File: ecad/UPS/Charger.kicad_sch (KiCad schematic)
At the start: 65 parts, among them J1 Barrel_Jack, J2 Conn_01x02_Socket, Q1 Q_PMOS, Q2 Q_PMOS_DGS, Q6 Q_NMOS_GDS, Q7 Q_NMOS_GDS, Q8 Q_NMOS_GDS, Q9 Q_NMOS_GDS, U1 BQ25730RSNR

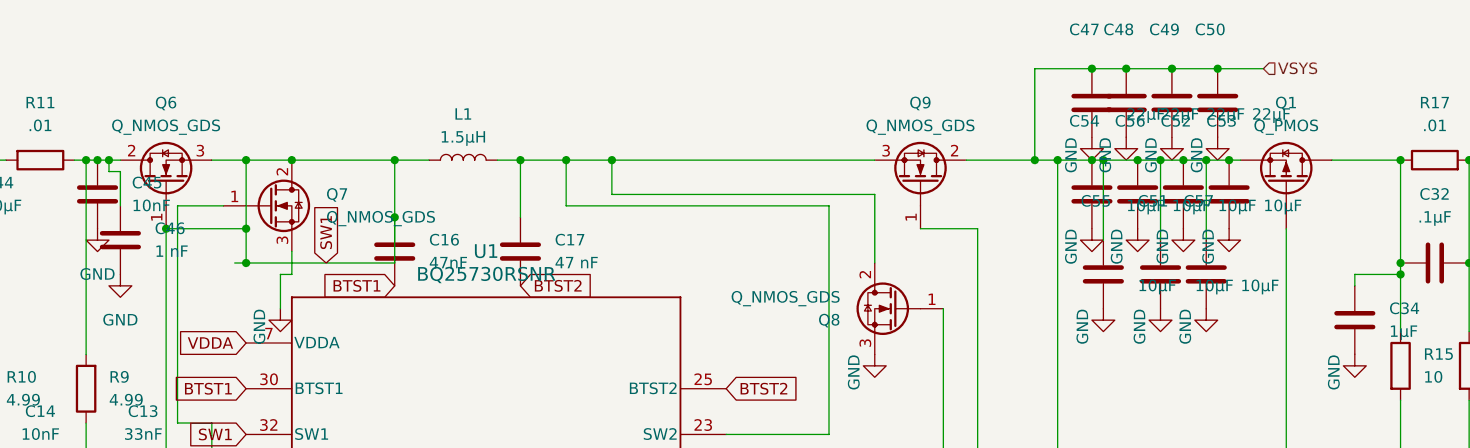
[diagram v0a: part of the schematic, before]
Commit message: Moved most components where they belong-ish
Barrel Jack's on the end as well as battery connector for now.  The MOSFET's need to be really close to the caps in the charger module
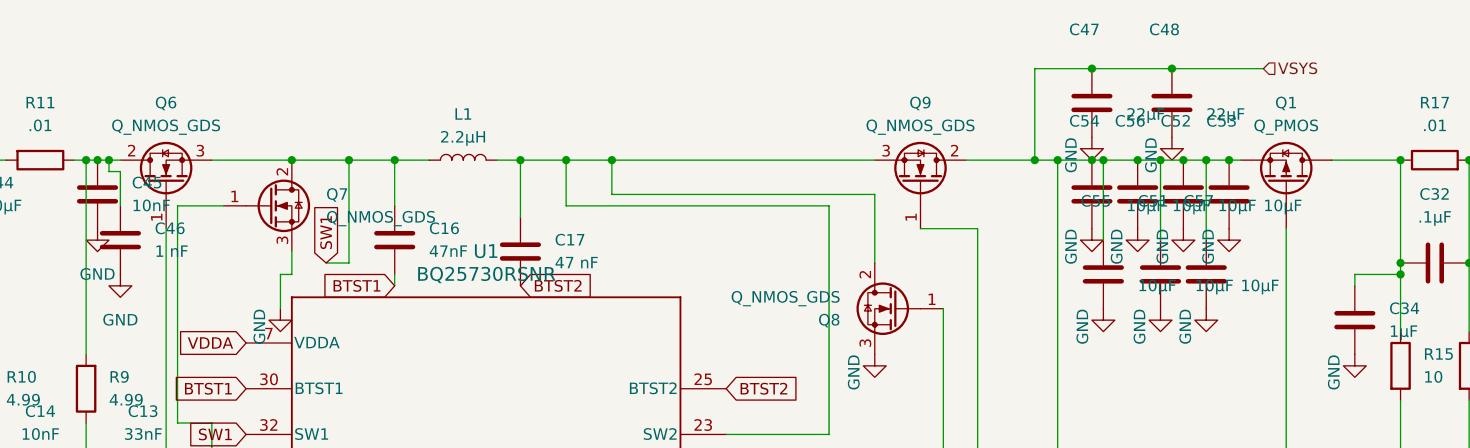
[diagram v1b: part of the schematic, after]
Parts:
- removed C49, C50: 22µF, Capacitor_SMD:C_1206_3216Metric, symbol Device:C
- D7: footprint (none) -> Diode_SMD:D_SMB_Handsoldering
- J1: footprint (none) -> Connector_BarrelJack:BarrelJack_Horizontal
- J2: footprint (none) -> Connector_AMASS:AMASS_XT60-F_1x02_P7.20mm_Vertical
- L1: value 1.5µH -> 2.2µH; footprint (none) -> Inductor_SMD:L_Vishay_IHLP-4040
- Q1, Q2: footprint (none) -> UPS:DNK0008A
- Q6, Q7, Q8, Q9: footprint (none) -> UPS:Ty's N Channel
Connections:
- net SW1: no longer Q6.1 (G), U1.31 (HIDRV1)
- new net: Q6.1 (G), U1.31 (HIDRV1)
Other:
- moved on the sheet: C16, C48

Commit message: More PCB Progress, more to come tomorrow morning
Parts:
- removed Q1: Q_PMOS, UPS:DNK0008A, symbol Device:Q_PMOS
- added B1, B2, B3, B4: 1121, UPS:1121_KEY, symbol UPS:1121
- added Q4: Q_PMOS_DGS, FDS6681Z_OSI, symbol UPS:FDS6681Z
- Q2: footprint UPS:DNK0008A -> FDS6681Z_OSI; symbol Transistor_FET:Q_PMOS_DGS -> UPS:FDS6681Z
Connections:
- net GND: now also Q6.1 (G), U1.31 (HIDRV1), B1.1, B2.1, B3.1, B4.1
- net at C32.1, C33.1, C37.1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: now also B1.2, B2.2, B3.2, B4.2
- net at J1.1: now also Q2.5, Q2.6, Q2.7, Q2.8; no longer Q2.1 (D)
- net at D7.2 (A), R27.2: now also Q2.4; no longer Q2.2 (G)
- net PMOS_IN_GATE: now reaches C39.1, C40.1, C41.1, C42.1, C43.1, C44.1, D7.1 (K), Q2.3, R10.2, R11.2, R12.2, U1.1 (VBUS)
- net PMOS_IN_GATE: now also C45.1, C46.1, Q2.1, Q2.2, Q6.2 (D), R11.1, R9.2
- net at C32.2, C34.1, R15.1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: now also Q4.5, Q4.6, Q4.7, Q4.8
- net at U1.21 (BATDRV_N): now also Q4.4
- net VSYS renamed PMOS_OUT_GATE
- net PMOS_OUT_GATE: now also Q4.1, Q4.2, Q4.3
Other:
- moved on the sheet: C1, C16, C17, C2, C32, C33, C34, C37, C47, C48, C51, C52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

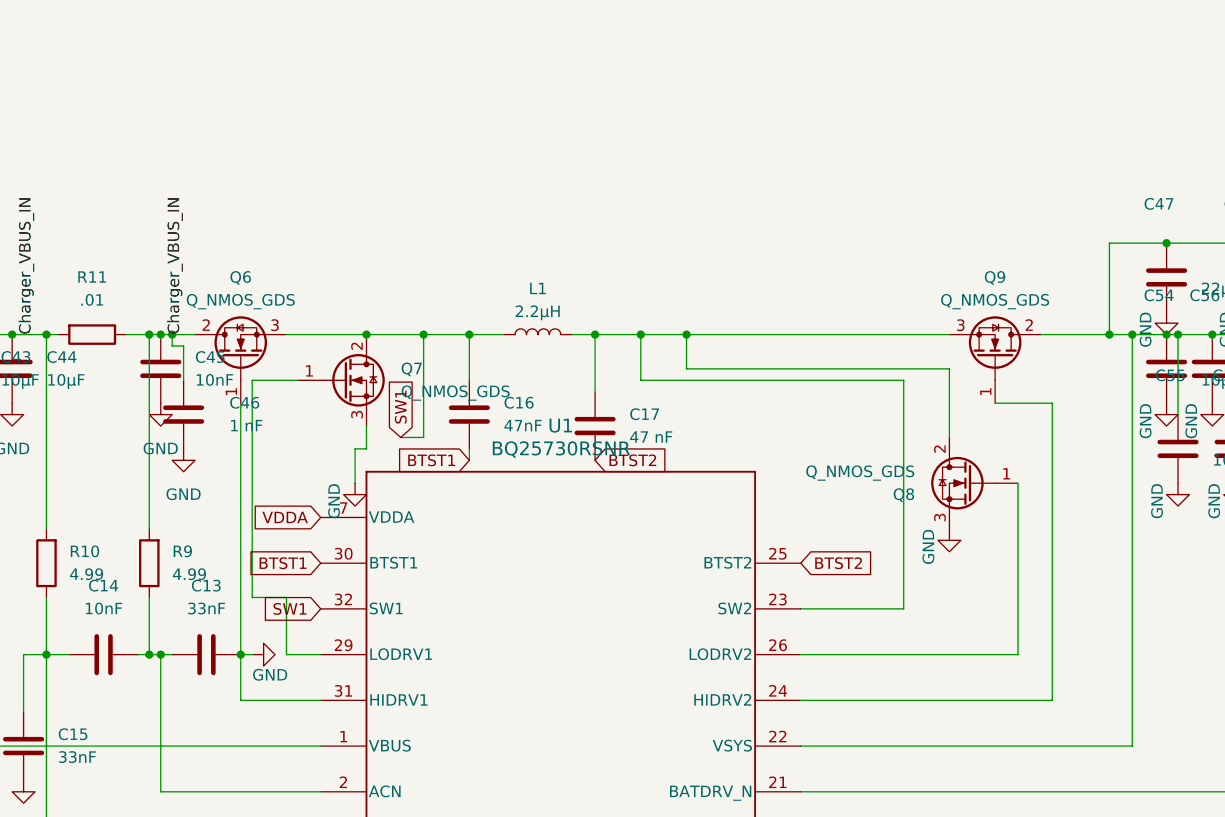
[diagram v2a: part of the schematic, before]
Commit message: Last minute footprint fixes on charger module
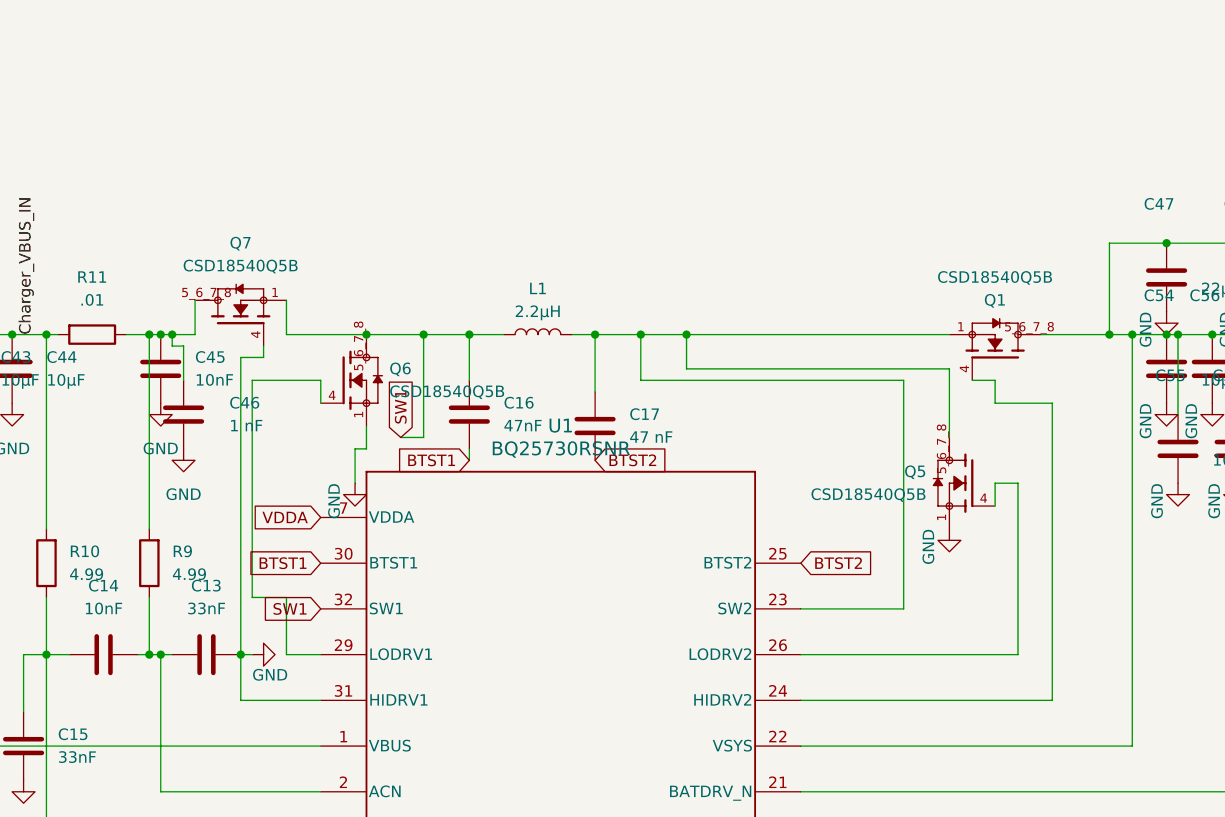
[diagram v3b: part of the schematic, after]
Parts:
- removed Q6, Q7, Q8, Q9: Q_NMOS_GDS, UPS:Ty's N Channel, symbol Transistor_FET:Q_NMOS_GDS
- added Q1, Q5, Q6, Q7: CSD18540Q5B, UPS:TRANS_CSD18540Q5B, symbol UPS:CSD18540Q5B
- Q2, Q4: footprint FDS6681Z_OSI -> UPS:FDS6681Z_OSI-M
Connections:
- net GND: now also Q5.1, Q5.2, Q5.3, Q6.1, Q6.2, Q6.3, Q7.4
- net PMOS_IN_GATE: no longer C45.1, C46.1, R11.1, R9.2
- net PMOS_OUT_GATE: now also Q1.5_6_7_8
- net SW1: now also Q6.5_6_7_8, Q7.1, Q7.2, Q7.3
- net at U1.24 (HIDRV2): now also Q1.4
- net at C17.2, L1.2, U1.23 (SW2): now also Q1.1, Q1.2, Q1.3, Q5.5_6_7_8
- net at U1.29 (LODRV1): now also Q6.4
- net at U1.26 (LODRV2): now also Q5.4
- new net: C45.1, C46.1, Q7.5_6_7_8, R11.1, R9.2

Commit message: Need to finish some traces, DRC warnings are keeping me from routing to the BQ,
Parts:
- removed R10, R9: 4.99, Resistor_SMD:R_0805_2012Metric, symbol Device:R
- removed R15, R16: 10, Resistor_SMD:R_0805_2012Metric, symbol Device:R
- added R24, R28, R34: 68.1k, Resistor_SMD:R_0805_2012Metric_Pad1.20x1.40mm_HandSolder, symbol Device:R
- added TH2, TH3, TH4: B57471V2104J062, Resistor_SMD:R_0805_2012Metric_Pad1.20x1.40mm_HandSolder, symbol Device:Thermistor_NTC
- C27: value .000001 -> 1uF
- C30: value 680 pF -> 1200 pF
- C31: value 4.7nF -> 3.3nF
- Q4: footprint UPS:FDS6681Z_OSI-M -> UPS:FDS6681Z_OSI
- R1: value 191k -> 140k
- R13: value 40.2k -> 16.9k
- R14: value 15k -> 10k
- R2: value 30k -> 10k
- R3: value 380k -> 56k
- R4: value 220k -> 100k
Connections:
- net GND: now also TH2.2, TH3.2, TH4.2
- net PMOS_IN_GATE: now also C14.1, C15.2, U1.3 (ACP)
- net at B1.2, B2.2, B3.2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: now also U1.19 (SRN)
- net at C13.1, C14.2, U1.2 (ACN): now also C45.1, C46.1, Q7.5_6_7_8, R11.1
- net at C32.2, C34.1, Q4.5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: now also U1.20 (SRP)
- new net +3.3V: R24.1, R28.1, R34.1
- new net bat_th1: R24.2, TH2.1
- new net bat_th2: R28.2, TH3.1
- new net bat_th3: R34.2, TH4.1
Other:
- moved on the sheet: B1, B2, B3, B4, C1, C13, C14, C15, C16, C17, C2, C27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
